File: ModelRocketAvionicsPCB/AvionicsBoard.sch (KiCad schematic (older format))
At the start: 38 parts

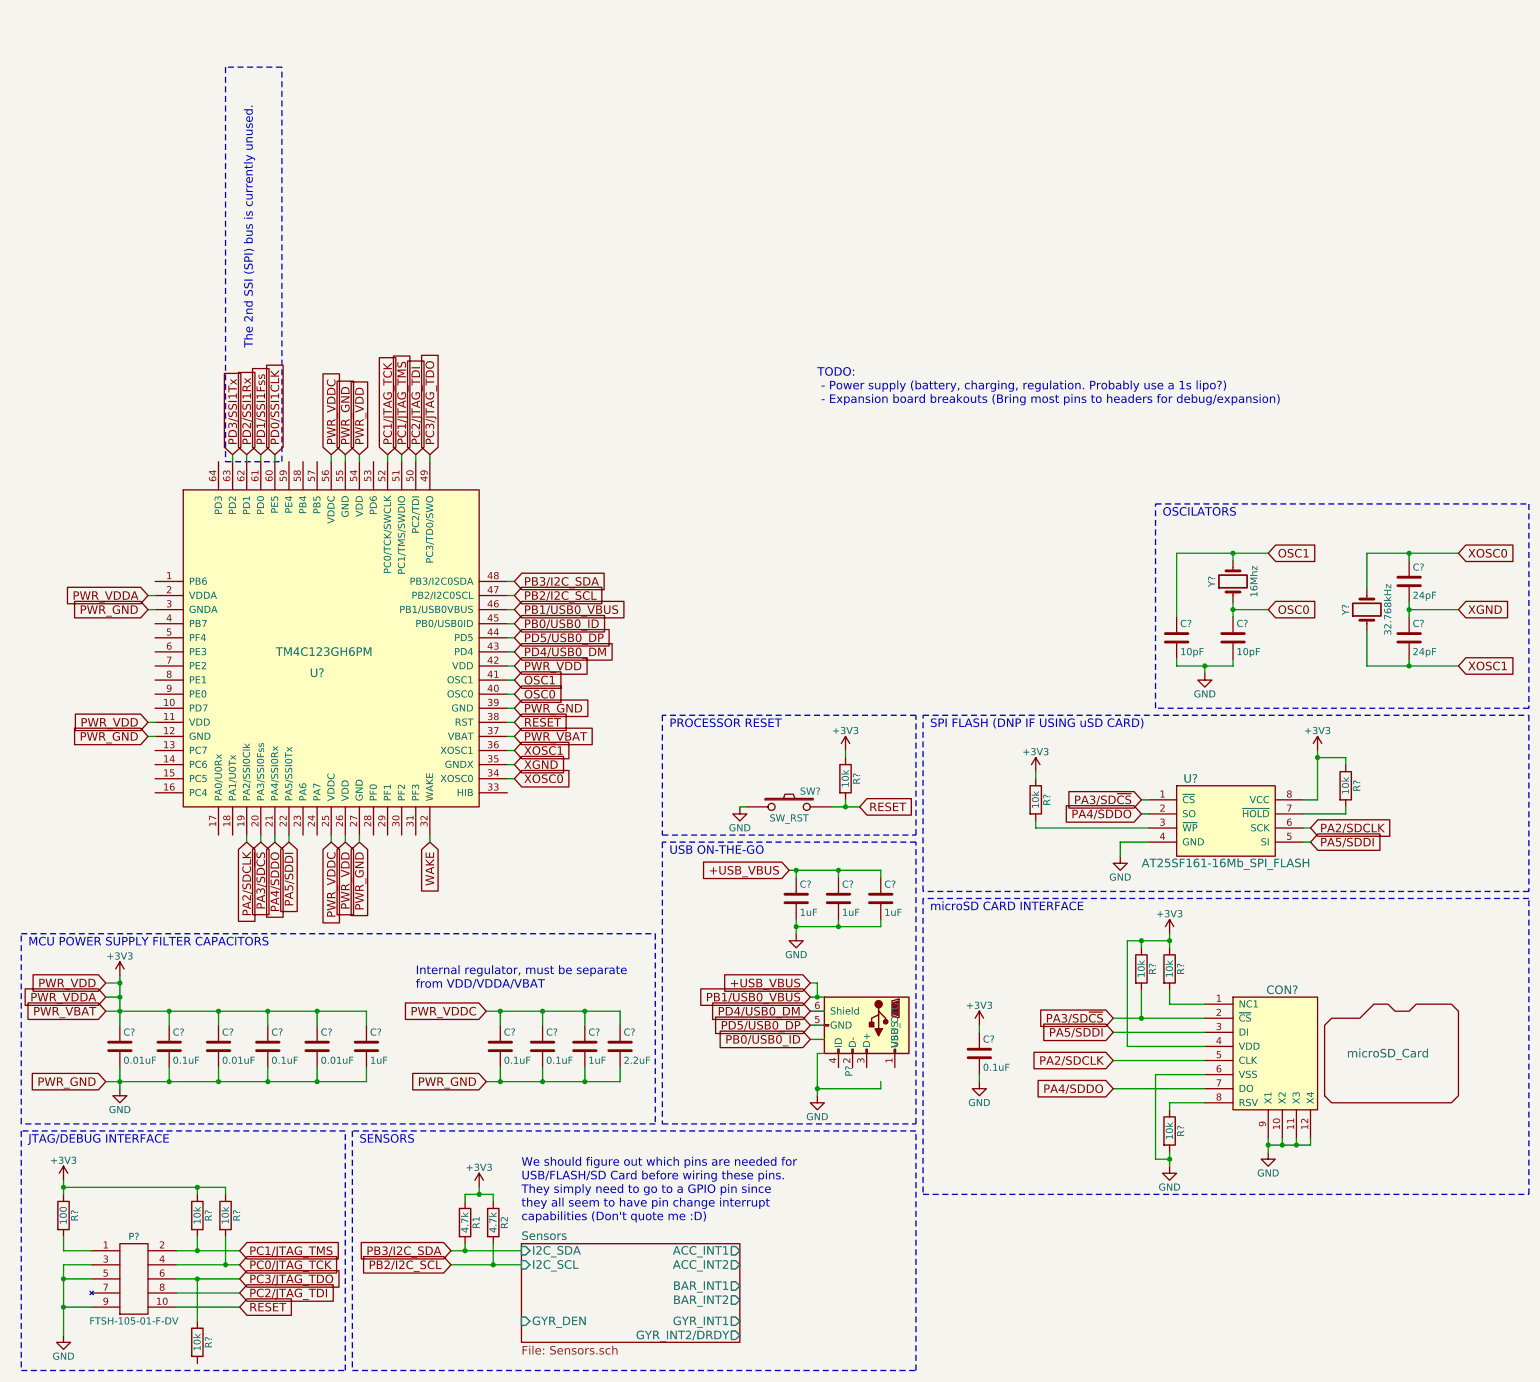
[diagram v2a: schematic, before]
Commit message: Critical features/components of avionics board schematic are complete (needs review). Still need to figure out a logical expansion header pinout and place the headers.
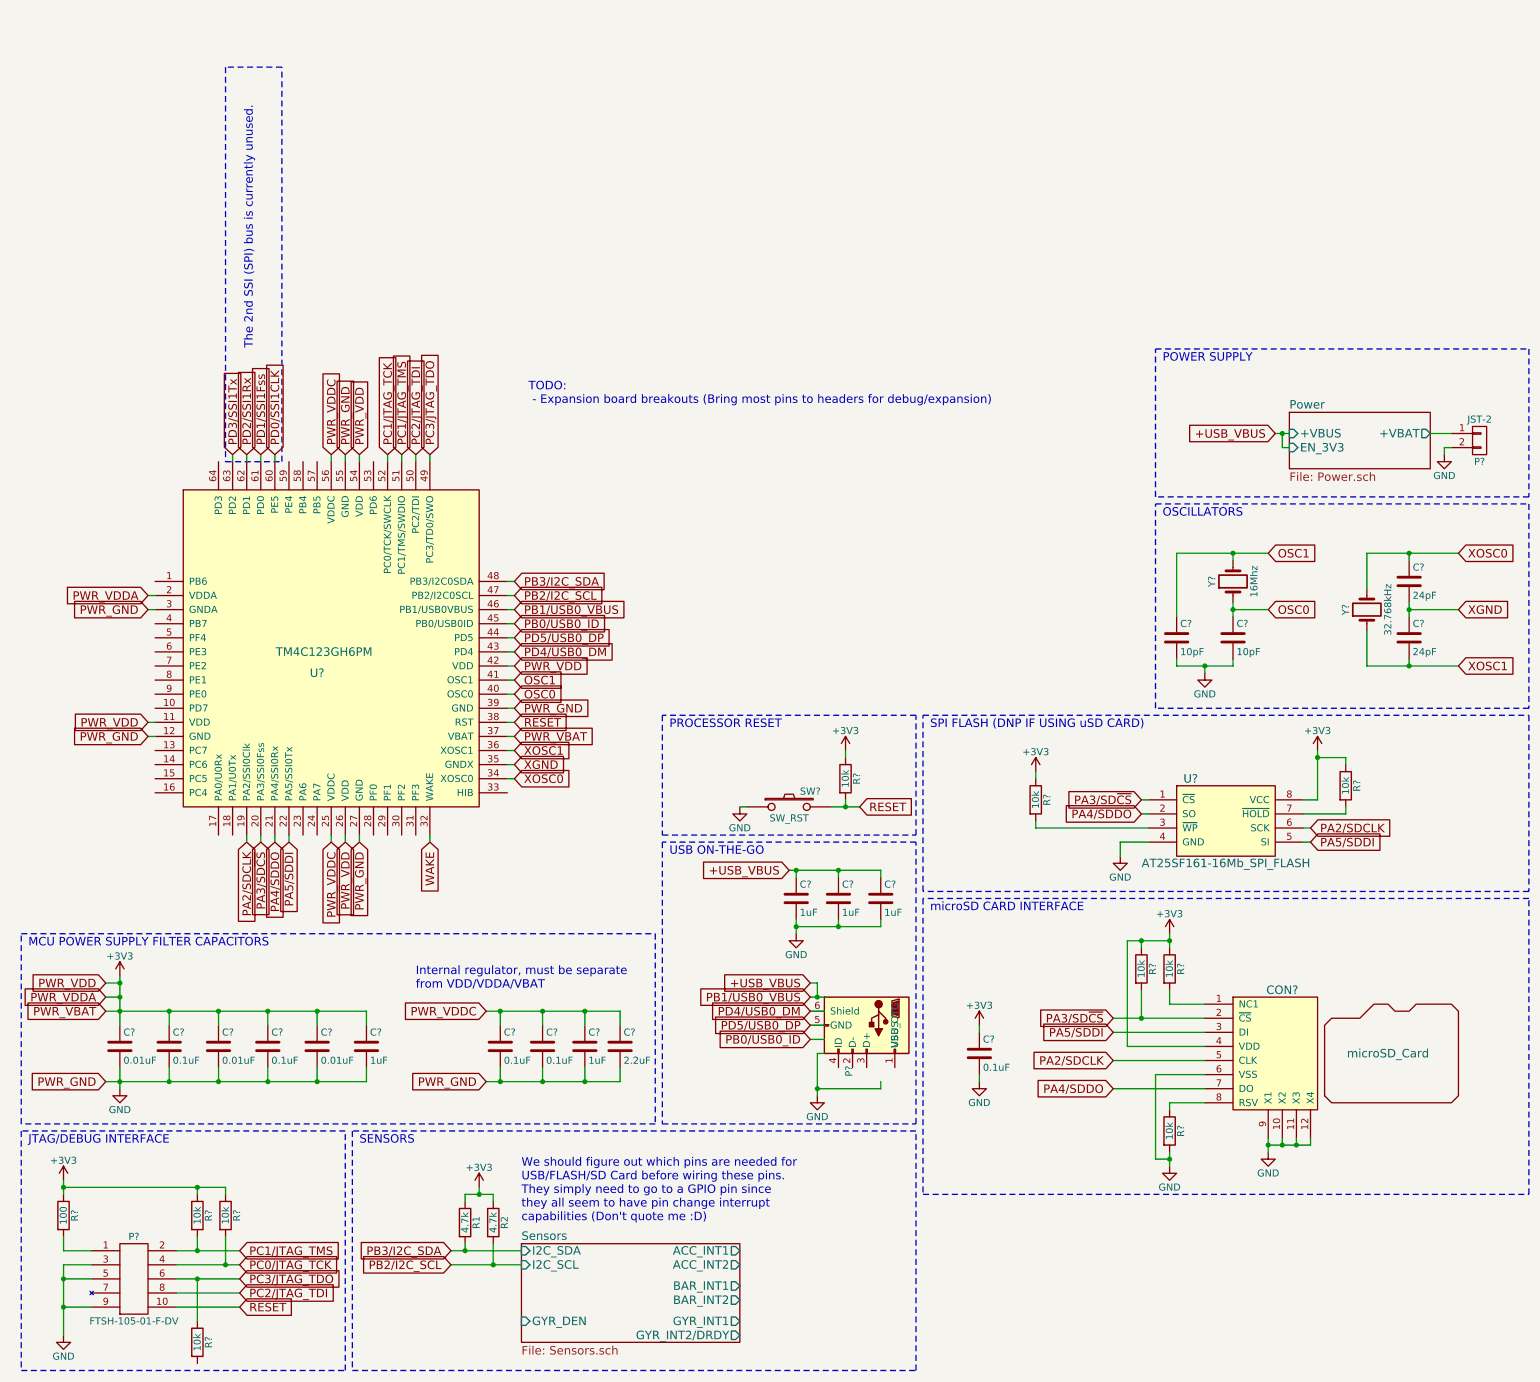
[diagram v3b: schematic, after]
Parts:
- added P?: JST-2, symbol CONN_01X02
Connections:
- net GND: now also P?.2 (P2)
- new net Power/+VBAT: P?.1 (P1)
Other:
- note added: "OSCILLATORS"
- note added: "POWER SUPPLY"
- note added: "TODO:\n - Expansion board breakouts (Bring most pins to headers for debug/expansion)\n"
- note removed: "OSCILATORS"
- note removed: "TODO:\n - Power supply (battery, charging, regulation. Probably use a 1s lipo?)\n - Expansion board breakouts (Bring most pins to headers for debug/expansion)\n"
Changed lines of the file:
@@
 $Descr A4 11693 8268
 encoding utf-8
-Sheet 1 2
+Sheet 1 3
 Title ""
 Date ""
@@
 	800  7300 1000 7300
 Wire Wire Line
-	800  7000 800  7100
-Wire Wire Line
-	800  7100 800  7300
-Wire Wire Line
-	800  7300 800  7500
+	800  7000 800  7500
 Wire Wire Line
 	1000 7100 800  7100
@@
 Connection ~ 800  7100
 Wire Wire Line
-	800  6400 800  6450
-Wire Wire Line
-	800  6450 800  6500
+	800  6400 800  6500
 Wire Wire Line
 	1750 7400 1750 7100
 Wire Wire Line
-	1600 7100 1750 7100
-Wire Wire Line
-	1750 7100 2050 7100
+	1600 7100 2050 7100
 Wire Wire Line
 	1750 6800 1750 6900
 Wire Wire Line
-	1600 6900 1750 6900
-Wire Wire Line
-	1750 6900 2050 6900
-Wire Wire Line
-	1600 7000 1950 7000
-Wire Wire Line
-	1950 7000 2050 7000
+	1600 6900 2050 6900
+Wire Wire Line
+	1600 7000 2050 7000
 Wire Wire Line
 	1950 7000 1950 6800
@@
 Connection ~ 1750 7100
 Wire Wire Line
-	800  6450 1750 6450
-Wire Wire Line
-	1750 6450 1950 6450
+	800  6450 1950 6450
 Wire Wire Line
 	1950 6450 1950 6500
@@
 	3400 1300 3400 1250
 Wire Wire Line
-	3550 6900 3650 6900
-Wire Wire Line
-	3650 6900 4050 6900
-Wire Wire Line
-	3550 7000 3850 7000
-Wire Wire Line
-	3850 7000 4050 7000
+	3550 6900 4050 6900
+Wire Wire Line
+	3550 7000 4050 7000
 Wire Wire Line
 	3650 6550 3650 6500
 Wire Wire Line
-	3650 6500 3750 6500
-Wire Wire Line
-	3750 6500 3850 6500
+	3650 6500 3850 6500
 Wire Wire Line
 	3750 6500 3750 6450
@@
 Connection ~ 1200 5100
 Wire Wire Line
-	1100 5700 1200 5700
-Wire Wire Line
-	1200 5700 1550 5700
-Wire Wire Line
-	1550 5700 1900 5700
-Wire Wire Line
-	1900 5700 2250 5700
-Wire Wire Line
-	2250 5700 2600 5700
-Wire Wire Line
-	2600 5700 2950 5700
+	1100 5700 2950 5700
 Wire Wire Line
 	1550 5700 1550 5600
@@
 Connection ~ 2600 5700
 Wire Wire Line
-	1200 5600 1200 5700
-Wire Wire Line
-	1200 5700 1200 5750
+	1200 5600 1200 5750
 Connection ~ 1200 5700
 Wire Wire Line
-	1200 4950 1200 5000
-Wire Wire Line
-	1200 5000 1200 5100
-Wire Wire Line
-	1200 5100 1200 5200
-Wire Wire Line
-	1200 5200 1200 5300
+	1200 4950 1200 5300
 Connection ~ 1200 5200
 Wire Wire Line
 	2950 5200 2950 5300
 Wire Wire Line
-	1100 5200 1200 5200
-Wire Wire Line
-	1200 5200 1550 5200
-Wire Wire Line
-	1550 5200 1900 5200
-Wire Wire Line
-	1900 5200 2250 5200
-Wire Wire Line
-	2250 5200 2600 5200
-Wire Wire Line
-	2600 5200 2950 5200
+	1100 5200 2950 5200
 Wire Wire Line
 	1550 5300 1550 5200
@@
 Connection ~ 2600 5200
 Wire Wire Line
-	3800 5200 3900 5200
-Wire Wire Line
-	3900 5200 4200 5200
-Wire Wire Line
-	4200 5200 4500 5200
-Wire Wire Line
-	4500 5200 4750 5200
+	3800 5200 4750 5200
 Wire Wire Line
 	3900 5200 3900 5300
@@
 	3900 5600 3900 5700
 Wire Wire Line
-	3800 5700 3900 5700
-Wire Wire Line
-	3900 5700 4200 5700
-Wire Wire Line
-	4200 5700 4500 5700
-Wire Wire Line
-	4500 5700 4750 5700
+	3800 5700 4750 5700
 Wire Wire Line
 	4200 5700 4200 5600
@@
 	5000 6000 500  6000
 Wire Wire Line
-	9350 6100 9350 6150
-Wire Wire Line
-	9350 6150 9350 6200
+	9350 6100 9350 6200
 Wire Wire Line
 	9450 6100 9450 6150
 Wire Wire Line
-	9350 6150 9450 6150
-Wire Wire Line
-	9450 6150 9550 6150
-Wire Wire Line
-	9550 6150 9650 6150
+	9350 6150 9650 6150
 Connection ~ 9350 6150
 Wire Wire Line
@@
 	8450 5050 8450 5250
 Wire Wire Line
-	8250 5250 8450 5250
-Wire Wire Line
-	8450 5250 8900 5250
+	8250 5250 8900 5250
 Wire Wire Line
 	8900 5450 8350 5450
@@
 	8550 6250 8650 6250
 Wire Wire Line
-	8650 6200 8650 6250
-Wire Wire Line
-	8650 6250 8650 6300
+	8650 6200 8650 6300
 Connection ~ 8650 6250
 Wire Wire Line
-	8650 4650 8650 4700
-Wire Wire Line
-	8650 4700 8650 4750
-Wire Wire Line
-	8350 4700 8450 4700
-Wire Wire Line
-	8450 4700 8650 4700
+	8650 4650 8650 4750
+Wire Wire Line
+	8350 4700 8650 4700
 Connection ~ 8450 4700
 Connection ~ 8650 4700
@@
 	9700 3700 9600 3700
 Wire Wire Line
-	9700 3350 9700 3400
-Wire Wire Line
-	9700 3400 9700 3700
+	9700 3350 9700 3700
 Wire Wire Line
 	8500 4000 8300 4000
@@
 	6150 5000 6150 5100
 Wire Wire Line
-	6100 5100 6150 5100
-Wire Wire Line
-	6150 5100 6200 5100
+	6100 5100 6200 5100
 Connection ~ 6150 5100
 Wire Wire Line
-	6150 5500 6150 5750
-Wire Wire Line
-	6150 5750 6150 5800
+	6150 5500 6150 5800
 Wire Wire Line
 	6150 5500 6200 5500
@@
 $EndComp
 Wire Wire Line
-	6000 4550 6000 4600
-Wire Wire Line
-	6000 4600 6000 4650
+	6000 4550 6000 4650
 $Comp
 L C C?
@@
 $EndComp
 Wire Wire Line
-	6000 4600 6300 4600
-Wire Wire Line
-	6300 4600 6600 4600
+	6000 4600 6600 4600
 Wire Wire Line
 	6300 4600 6300 4550
@@
 Connection ~ 6300 4600
 Wire Wire Line
-	5950 4200 6000 4200
-Wire Wire Line
-	6000 4200 6300 4200
-Wire Wire Line
-	6300 4200 6600 4200
+	5950 4200 6600 4200
 Wire Wire Line
 	6000 4200 6000 4250
@@
 Text Notes 5100 4100 0    60   ~ 0
 USB ON-THE-GO
-Text Notes 6150 900  0    60   ~ 0
-TODO:\n - Power supply (battery, charging, regulation. Probably use a 1s lipo?)\n - Expansion board breakouts (Bring most pins to headers for debug/expansion)\n
+Text Notes 4100 900  0    60   ~ 0
+TODO:\n - Expansion board breakouts (Bring most pins to headers for debug/expansion)\n
 Text Notes 2150 500  1    60   ~ 0
 The 2nd SSI (SPI) bus is currently unused.
@@
 $EndComp
 Wire Wire Line
-	8700 1950 9100 1950
-Wire Wire Line
-	9100 1950 9350 1950
+	8700 1950 9350 1950
 Wire Wire Line
 	9100 1950 9100 2000
@@
 	8700 1950 8700 2400
 Wire Wire Line
-	9100 2300 9100 2350
-Wire Wire Line
-	9100 2350 9100 2400
+	9100 2300 9100 2400
 Wire Wire Line
 	9350 2350 9100 2350
@@
 	8900 2800 8900 2750
 Wire Wire Line
-	8700 2750 8900 2750
-Wire Wire Line
-	8900 2750 9100 2750
+	8700 2750 9100 2750
 Wire Wire Line
 	8700 2750 8700 2700
@@
 	10700 2350 10350 2350
 Wire Wire Line
-	10350 2300 10350 2350
-Wire Wire Line
-	10350 2350 10350 2400
+	10350 2300 10350 2400
 Connection ~ 10350 2350
 Wire Wire Line
-	10050 2750 10350 2750
-Wire Wire Line
-	10350 2750 10700 2750
+	10050 2750 10700 2750
 Wire Wire Line
 	10350 2750 10350 2700
@@
 	10050 2200 10050 1950
 Wire Wire Line
-	10050 1950 10350 1950
-Wire Wire Line
-	10350 1950 10700 1950
+	10050 1950 10700 1950
 Wire Wire Line
 	10350 2000 10350 1950
@@
 	11200 3050 8550 3050
 Text Notes 8600 1700 0    60   ~ 0
-OSCILATORS
+OSCILLATORS
 Wire Wire Line
 	4000 3350 3950 3350
@@
 RESET
 Wire Wire Line
-	6250 3750 6350 3750
-Wire Wire Line
-	6350 3750 6450 3750
+	6250 3750 6450 3750
 Wire Wire Line
 	6350 3750 6350 3700
@@
 Text Notes 5100 3200 0    60   ~ 0
 PROCESSOR RESET
+$Sheet
+S 9500 950  1000 400
+U 5AE8FB66
+F0 "Power" 60
+F1 "Power.sch" 60
+F2 "+VBUS" I L 9500 1100 60
+F3 "EN_3V3" I L 9500 1200 60
+F4 "+VBAT" O R 10500 1100 60
+$EndSheet
+$Comp
+L CONN_01X02 P?
+U 1 1 5AE964AC
+P 10850 1150
+F 0 "P?" H 10850 1000 50  0000 C CNN
+F 1 "JST-2" H 10850 1300 50  0000 C CNN
+F 2 "" H 10850 1150 50  0000 C CNN
+F 3 "" H 10850 1150 50  0000 C CNN
+	1    10850 1150
+	1    0    0    -1
+$EndComp
+Wire Wire Line
+	10500 1100 10650 1100
+$Comp
+L GND #PWR?
+U 1 1 5AE96FA7
+P 10600 1250
+F 0 "#PWR?" H 10600 1000 50  0001 C CNN
+F 1 "GND" H 10600 1100 50  0000 C CNN
+F 2 "" H 10600 1250 50  0000 C CNN
+F 3 "" H 10600 1250 50  0000 C CNN
+	1    10600 1250
+	1    0    0    -1
+$EndComp
+Wire Wire Line
+	10600 1250 10600 1200
+Wire Wire Line
+	10600 1200 10650 1200
+Text GLabel 9400 1100 0    60   Input ~ 0
++USB_VBUS
+Wire Wire Line
+	9400 1100 9500 1100
+Wire Wire Line
+	9450 1100 9450 1200
+Wire Wire Line
+	9450 1200 9500 1200
+Connection ~ 9450 1100
+Wire Notes Line
+	8550 1550 8550 500
+Wire Notes Line
+	8550 500  11200 500
+Wire Notes Line
+	11200 500  11200 1550
+Wire Notes Line
+	11200 1550 8550 1550
+Text Notes 8600 600  0    60   ~ 0
+POWER SUPPLY
 $EndSCHEMATC

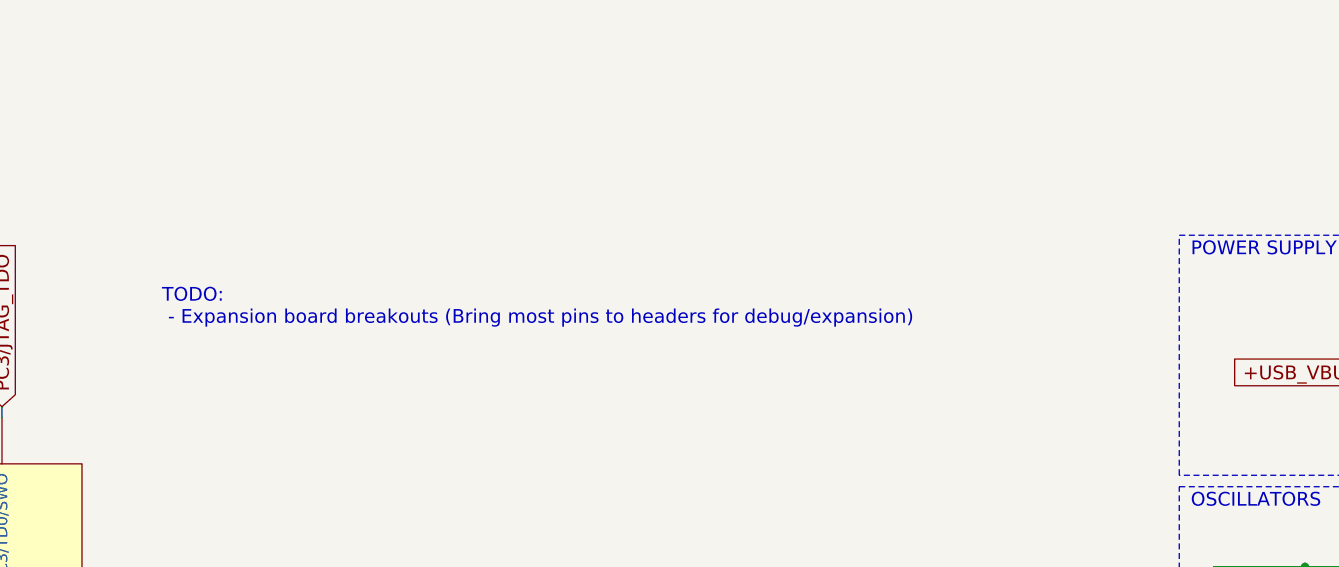
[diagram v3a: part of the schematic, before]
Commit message: Added IMU interrupt pin wiring to TODO and created a basic PDF of the current schematic
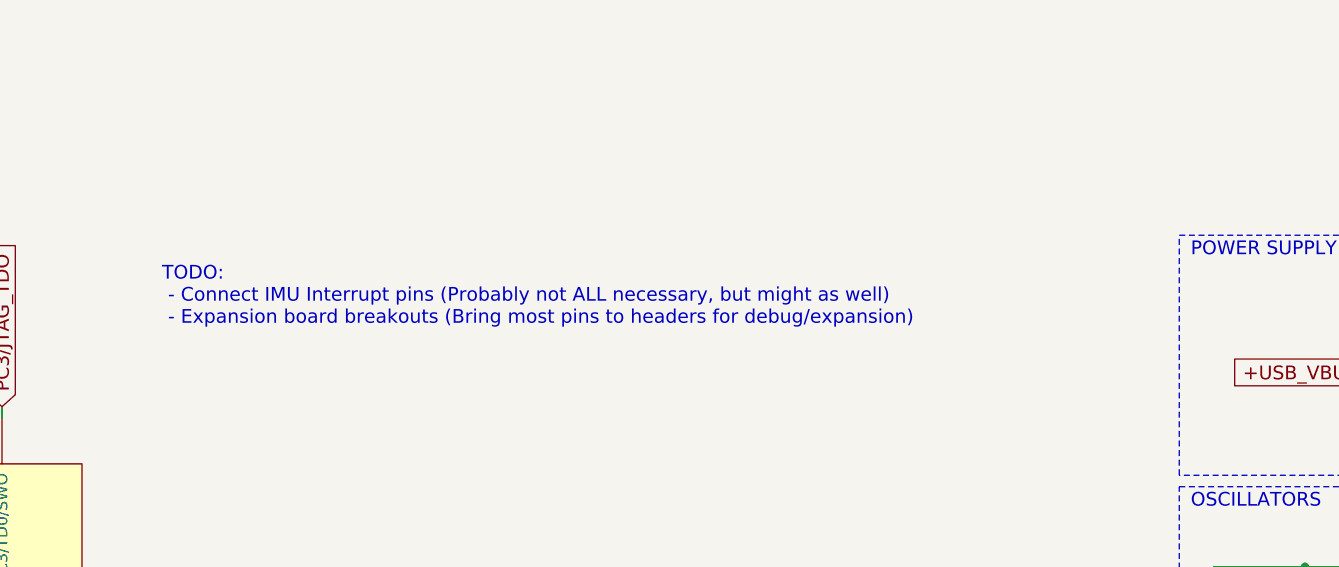
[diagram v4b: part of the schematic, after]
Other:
- note added: "TODO:\n - Connect IMU Interrupt pins (Probably not ALL necessary, but might as well)\n - Expansion board breakouts (Bring most pins to headers for debug/expansion)\n"
- note removed: "TODO:\n - Expansion board breakouts (Bring most pins to headers for debug/expansion)\n"
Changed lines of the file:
@@
 USB ON-THE-GO
 Text Notes 4100 900  0    60   ~ 0
-TODO:\n - Expansion board breakouts (Bring most pins to headers for debug/expansion)\n
+TODO:\n - Connect IMU Interrupt pins (Probably not ALL necessary, but might as well)\n - Expansion board breakouts (Bring most pins to headers for debug/expansion)\n
 Text Notes 2150 500  1    60   ~ 0
 The 2nd SSI (SPI) bus is currently unused.
